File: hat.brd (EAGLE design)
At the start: 65 x 56.5 mm, 44 parts, among them U1 ADS1115IDGST, U2 ADXL345, U3 MCP2515-I/SO, U4 MCP2551, X1 16Mhz

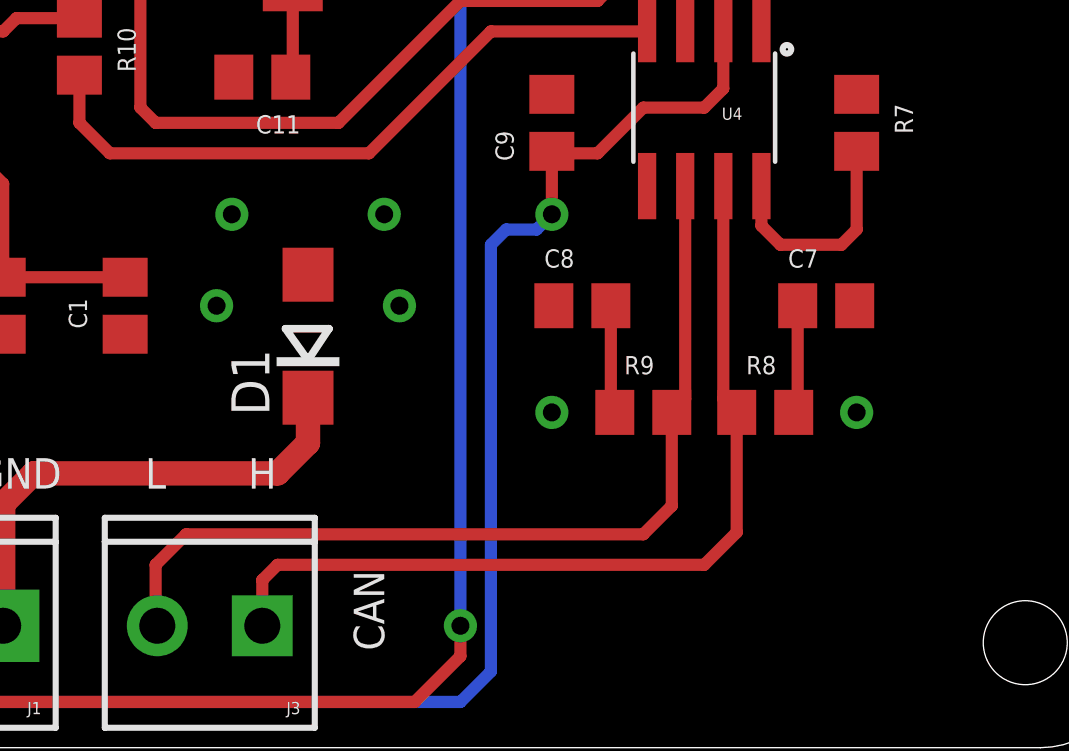
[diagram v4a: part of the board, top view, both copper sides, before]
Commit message: Tweaked spacing for two resistors
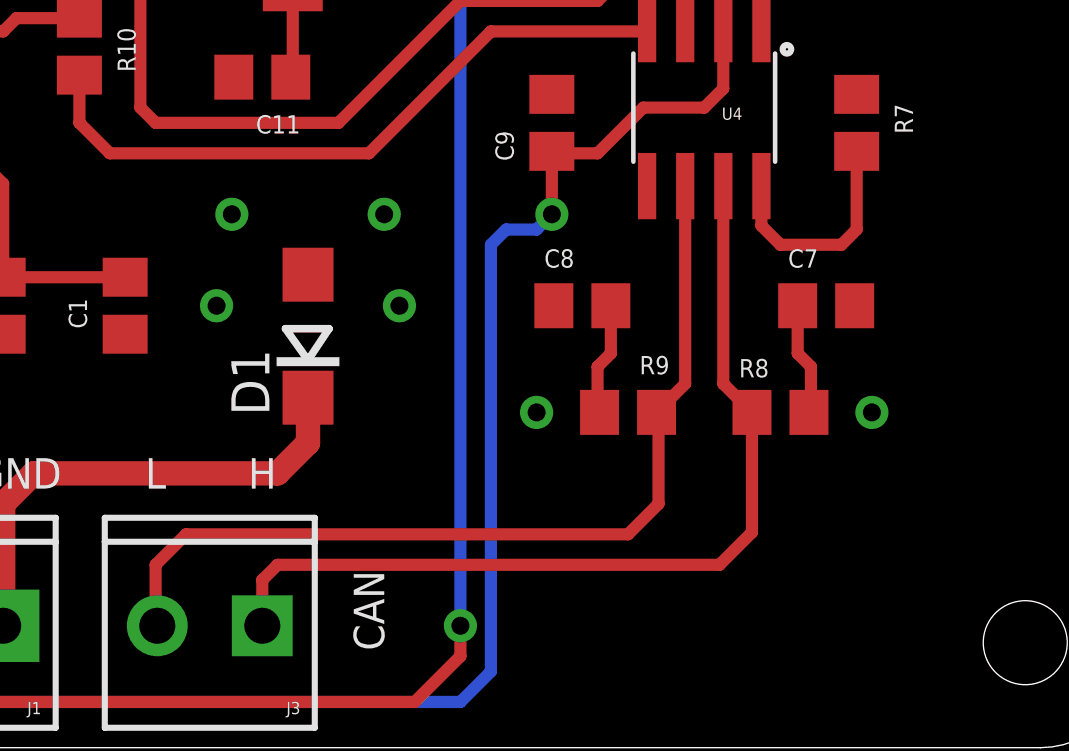
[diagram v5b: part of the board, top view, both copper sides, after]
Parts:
- moved R8 0.51 mm to (53.3, 11.2)
- moved R9 0.51 mm to (48.3, 11.2)
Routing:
- net CANH: track 29.7 -> 30.4 mm
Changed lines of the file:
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@@
 </element>
 <element name="R7" library="aceat64-passives" package="R0805" value="4k7" x="55.88" y="20.828" rot="R270"/>
-<element name="R8" library="aceat64-passives" package="R0805" value="100" x="52.832" y="11.176" smashed="yes" rot="R180">
-<attribute name="NAME" x="52.197" y="12.446" size="0.6096" layer="25"/>
-<attribute name="VALUE" x="52.197" y="9.906" size="0.6096" layer="27" align="top-left"/>
-</element>
-<element name="R9" library="aceat64-passives" package="R0805" value="100" x="48.768" y="11.176"/>
+<element name="R8" library="aceat64-passives" package="R0805" value="100" x="53.34" y="11.176" smashed="yes" rot="R180">
+<attribute name="NAME" x="52.959" y="12.954" size="0.6096" layer="25" rot="R180"/>
+<attribute name="VALUE" x="52.705" y="9.906" size="0.6096" layer="27" align="top-left"/>
+</element>
+<element name="R9" library="aceat64-passives" package="R0805" value="100" x="48.26" y="11.176" smashed="yes">
+<attribute name="NAME" x="48.641" y="12.446" size="0.6096" layer="25"/>
+<attribute name="VALUE" x="47.625" y="9.906" size="0.6096" layer="27" align="top-left"/>
+</element>
 <element name="FRAME2" library="SparkFun-Aesthetics" package="DUMMY" value="FRAME-LETTERNO_PACKAGE" x="0.508" y="0.508">
 <attribute name="DESIGNER" value="Nobody" x="0.508" y="0.508" size="1.778" layer="27" display="off"/>
@@
 <wire x1="8.636" y1="38.1" x2="8.636" y2="39.624" width="0.254" layer="1"/>
 <via x="6.096" y="16.764" extent="1-16" drill="0.6" shape="square"/>
-<via x="45.72" y="11.176" extent="1-16" drill="0.6" shape="square"/>
-<via x="55.88" y="11.176" extent="1-16" drill="0.6" shape="square"/>
+<via x="45.212" y="11.176" extent="1-16" drill="0.6" shape="square"/>
+<via x="56.388" y="11.176" extent="1-16" drill="0.6" shape="square"/>
 <via x="40.64" y="14.732" extent="1-16" drill="0.6" shape="square"/>
 <via x="51.308" y="40.64" extent="1-16" drill="0.6" shape="square"/>
@@
 <wire x1="36.068" y1="4.064" x2="36.068" y2="5.588" width="0.4064" layer="1"/>
 <wire x1="36.068" y1="5.588" x2="36.576" y2="6.096" width="0.4064" layer="1"/>
-<wire x1="36.576" y1="6.096" x2="50.8" y2="6.096" width="0.4064" layer="1"/>
-<wire x1="50.8" y1="6.096" x2="51.882" y2="7.178" width="0.4064" layer="1"/>
-<wire x1="51.882" y1="7.178" x2="51.882" y2="11.176" width="0.4064" layer="1"/>
-<wire x1="51.882" y1="11.176" x2="51.435" y2="11.623" width="0.4064" layer="1"/>
-<wire x1="51.435" y1="11.623" x2="51.435" y2="18.7198" width="0.4064" layer="1"/>
+<wire x1="36.576" y1="6.096" x2="51.308" y2="6.096" width="0.4064" layer="1"/>
+<wire x1="51.308" y1="6.096" x2="52.39" y2="7.178" width="0.4064" layer="1"/>
+<wire x1="52.39" y1="7.178" x2="52.39" y2="11.176" width="0.4064" layer="1"/>
+<wire x1="52.39" y1="11.176" x2="51.435" y2="12.131" width="0.4064" layer="1"/>
+<wire x1="51.435" y1="12.131" x2="51.435" y2="18.7198" width="0.4064" layer="1"/>
 </signal>
 <signal name="CANL">
@@
 <contactref element="R9" pad="2"/>
 <contactref element="J3" pad="2"/>
-<wire x1="48.768" y1="7.112" x2="33.528" y2="7.112" width="0.4064" layer="1"/>
 <wire x1="33.528" y1="7.112" x2="32.512" y2="6.096" width="0.4064" layer="1"/>
 <wire x1="32.512" y1="6.096" x2="32.512" y2="4.12" width="0.4064" layer="1"/>
 <wire x1="32.512" y1="4.12" x2="32.568" y2="4.064" width="0.4064" layer="1"/>
-<wire x1="48.768" y1="7.112" x2="49.718" y2="8.062" width="0.4064" layer="1"/>
-<wire x1="49.718" y1="8.062" x2="49.718" y2="11.176" width="0.4064" layer="1"/>
-<wire x1="49.718" y1="11.176" x2="50.165" y2="11.623" width="0.4064" layer="1"/>
-<wire x1="50.165" y1="11.623" x2="50.165" y2="18.7198" width="0.4064" layer="1"/>
+<wire x1="33.528" y1="7.112" x2="48.26" y2="7.112" width="0.4064" layer="1"/>
+<wire x1="48.26" y1="7.112" x2="49.276" y2="8.128" width="0.4064" layer="1"/>
+<wire x1="49.276" y1="8.128" x2="49.276" y2="11.11" width="0.4064" layer="1"/>
+<wire x1="49.276" y1="11.11" x2="49.21" y2="11.176" width="0.4064" layer="1"/>
+<wire x1="49.21" y1="11.176" x2="50.165" y2="12.131" width="0.4064" layer="1"/>
+<wire x1="50.165" y1="12.131" x2="50.165" y2="18.7198" width="0.4064" layer="1"/>
 </signal>
 <signal name="5V">
@@
 <signal name="N$6">
 <contactref element="R8" pad="1"/>
-<wire x1="53.782" y1="11.176" x2="53.914" y2="11.358" width="0.4064" layer="1"/>
+<wire x1="54.29" y1="11.176" x2="53.914" y2="11.358" width="0.4064" layer="1"/>
 <contactref element="C7" pad="1"/>
-<wire x1="53.782" y1="11.176" x2="53.914" y2="11.308" width="0.4064" layer="1"/>
-<wire x1="53.914" y1="11.308" x2="53.914" y2="14.732" width="0.4064" layer="1"/>
+<wire x1="53.914" y1="11.358" x2="54.356" y2="11.8" width="0.4064" layer="1"/>
+<wire x1="54.356" y1="11.8" x2="54.356" y2="12.7" width="0.4064" layer="1"/>
+<wire x1="54.356" y1="12.7" x2="53.914" y2="13.142" width="0.4064" layer="1"/>
+<wire x1="53.914" y1="13.142" x2="53.914" y2="14.732" width="0.4064" layer="1"/>
 </signal>
 <signal name="N$8">
 <contactref element="R9" pad="1"/>
-<wire x1="47.818" y1="11.176" x2="47.686" y2="11.358" width="0.4064" layer="1"/>
 <contactref element="C8" pad="1"/>
-<wire x1="47.686" y1="11.358" x2="47.686" y2="14.732" width="0.4064" layer="1"/>
+<wire x1="47.31" y1="11.176" x2="47.244" y2="11.242" width="0.4064" layer="1"/>
+<wire x1="47.244" y1="11.242" x2="47.244" y2="12.7" width="0.4064" layer="1"/>
+<wire x1="47.244" y1="12.7" x2="47.686" y2="13.142" width="0.4064" layer="1"/>
+<wire x1="47.686" y1="13.142" x2="47.686" y2="14.732" width="0.4064" layer="1"/>
 </signal>
 <signal name="N$4">

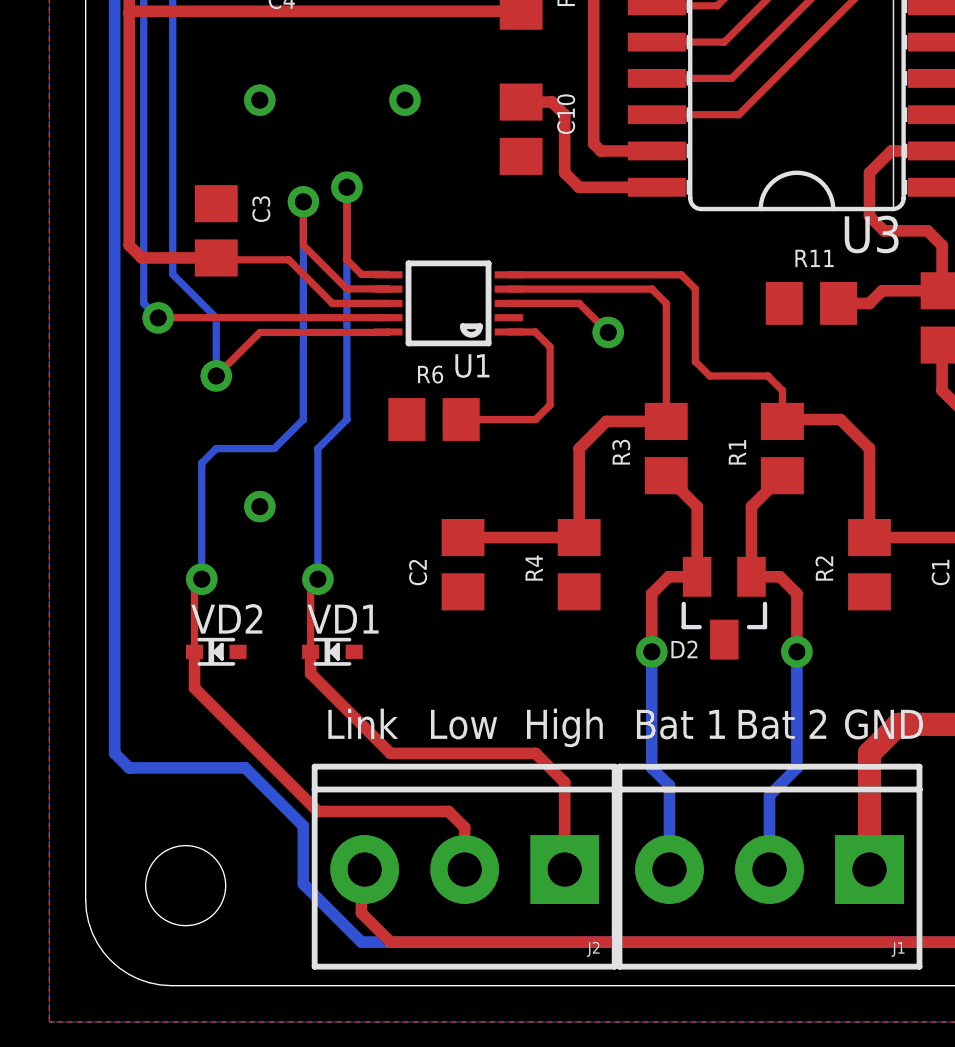
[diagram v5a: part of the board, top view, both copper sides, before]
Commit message: Replaced TVS diodes VD1/VD2 with single TVS diode D3
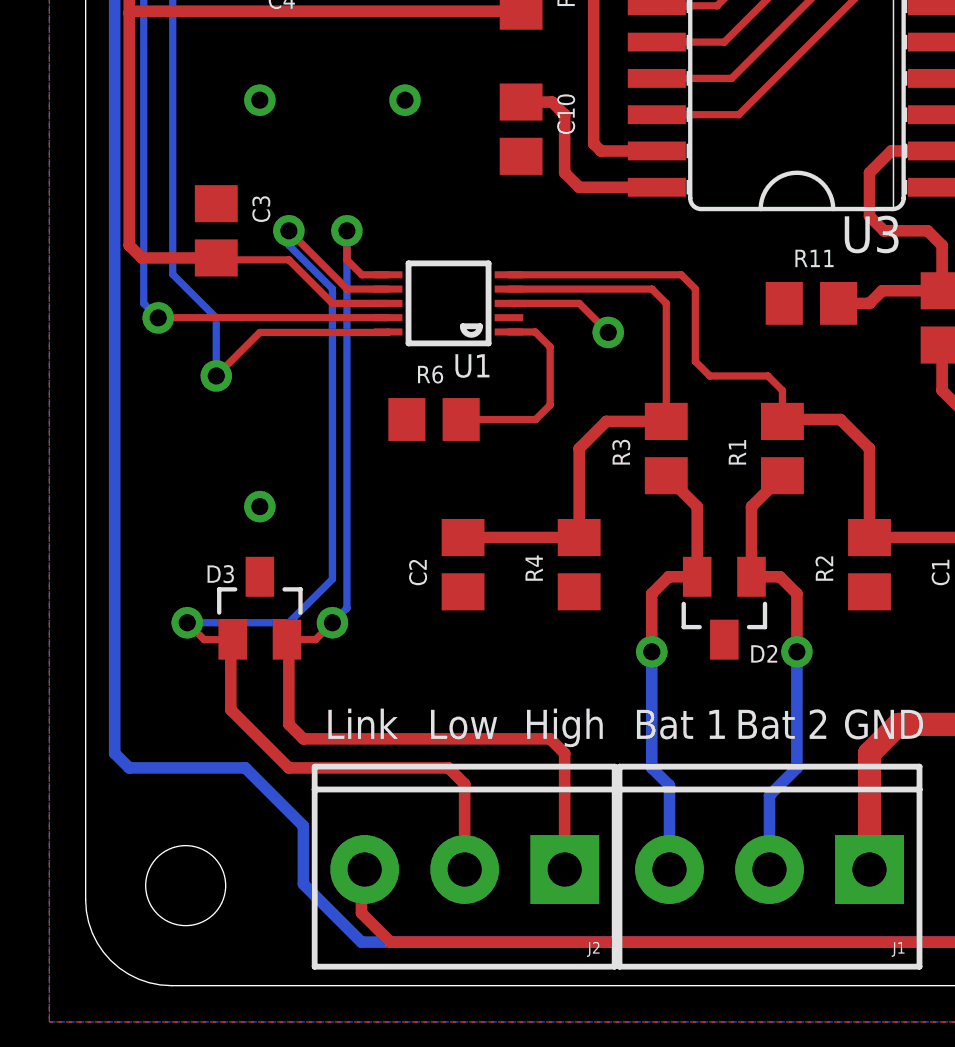
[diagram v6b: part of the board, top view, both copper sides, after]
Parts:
- removed VD1, VD2: (no value), diode:SOD523
- added D3: (no value), diode:SOT23
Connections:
- net GND: now also D3.3; no longer VD1.A, VD2.A
- net SHUNT-HIGH-INPUT: now also D3.2; no longer VD1.C
- net SHUNT-LOW-INPUT: now also D3.1; no longer VD2.C
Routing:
- net SHUNT-LOW-INPUT: track 37.9 -> 39.4 mm
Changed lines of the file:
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@@
 <element name="GPS" library="SparkFun-Connectors" package="1X05" value="" x="61.468" y="46.482" rot="R270"/>
 <element name="U2" library="SparkFun-Sensors" package="LGA14" value="ADXL345" x="11.684" y="40.64" rot="R90"/>
-<element name="U1" library="microbuilder" package="MSOP10" value="ADS1115IDGST" x="12.7" y="23.876" rot="R90"/>
+<element name="U1" library="microbuilder" package="MSOP10" value="ADS1115IDGST" x="12.7" y="23.876" smashed="yes" rot="R90">
+<attribute name="NAME" x="14.224" y="22.098" size="0.8128" layer="25" ratio="10" rot="R180"/>
+<attribute name="VALUE" x="10.16" y="25.908" size="0.8128" layer="27" ratio="10"/>
+</element>
 <element name="R5" library="aceat64-passives" package="R0805" value="4k7" x="42.672" y="33.02" rot="R90"/>
 <element name="R1" library="aceat64-resistor" package="R0805" value="4k7" x="24.384" y="18.796" rot="R90"/>
@@
 <element name="U3" library="mcp2515" package="SO18L" value="MCP2515-I/SO" x="24.892" y="33.02" rot="R90"/>
 <element name="D2" library="diode" package="SOT23" value="" x="22.352" y="13.208" smashed="yes" rot="R180">
-<attribute name="NAME" x="20.955" y="12.065" size="0.6096" layer="25" align="top-center"/>
+<attribute name="NAME" x="23.749" y="11.303" size="0.6096" layer="25" rot="R180" align="top-center"/>
 <attribute name="VALUE" x="24.257" y="16.383" size="1.27" layer="27" rot="R180"/>
 </element>
-<element name="VD1" library="diode" package="SOD523" value="" x="8.636" y="11.684"/>
-<element name="VD2" library="diode" package="SOD523" value="" x="4.572" y="11.684"/>
 <element name="J1" library="SparkFun-Connectors" package="SCREWTERMINAL-3.5MM-3" value="" x="27.432" y="4.064" rot="R180">
 <attribute name="PROD_ID" value="CONN-08288" x="27.432" y="4.064" size="1.778" layer="27" rot="R180" display="off"/>
@@
 <element name="C11" library="aceat64-passives" package="C0805" value="22pF" x="36.068" y="22.352" rot="R180"/>
 <element name="C12" library="aceat64-passives" package="C0805" value="22pF" x="36.068" y="40.64" rot="R180"/>
+<element name="D3" library="diode" package="SOT23" value="" x="6.096" y="13.208" smashed="yes">
+<attribute name="NAME" x="4.191" y="14.097" size="0.6096" layer="25"/>
+<attribute name="VALUE" x="4.191" y="10.033" size="1.27" layer="27"/>
+</element>
 </elements>
 <signals>
@@
 <via x="34.544" y="14.732" extent="1-16" drill="0.6" shape="square"/>
 <contactref element="D2" pad="3"/>
-<contactref element="VD2" pad="A"/>
-<contactref element="VD1" pad="A"/>
 <via x="8.636" y="38.1" extent="1-16" drill="0.6" shape="square"/>
 <via x="4.572" y="43.18" extent="1-16" drill="0.6" shape="square"/>
@@
 <contactref element="C11" pad="2"/>
 <contactref element="C12" pad="2"/>
+<contactref element="D3" pad="3"/>
 </signal>
 <signal name="TXD">
@@
 <signal name="SHUNT-HIGH-INPUT">
 <contactref element="U1" pad="6"/>
-<contactref element="VD1" pad="C"/>
-<wire x1="10.5869" y1="24.876" x2="10.5709" y2="24.892" width="0.254" layer="1"/>
-<wire x1="10.5709" y1="24.892" x2="9.652" y2="24.892" width="0.254" layer="1"/>
-<wire x1="9.652" y1="24.892" x2="9.144" y2="25.4" width="0.254" layer="1"/>
-<wire x1="9.144" y1="25.4" x2="9.144" y2="27.94" width="0.254" layer="1"/>
-<via x="9.144" y="27.94" extent="1-16" drill="0.6"/>
-<wire x1="9.144" y1="27.94" x2="9.144" y2="19.812" width="0.254" layer="16"/>
-<wire x1="9.144" y1="19.812" x2="8.128" y2="18.796" width="0.254" layer="16"/>
-<wire x1="8.128" y1="18.796" x2="8.128" y2="14.224" width="0.254" layer="16"/>
-<via x="8.128" y="14.224" extent="1-16" drill="0.6"/>
-<wire x1="8.128" y1="14.224" x2="7.874" y2="13.97" width="0.254" layer="1"/>
-<wire x1="7.874" y1="13.97" x2="7.874" y2="11.684" width="0.254" layer="1"/>
 <contactref element="J2" pad="1"/>
-<wire x1="7.874" y1="11.684" x2="7.874" y2="10.922" width="0.4064" layer="1"/>
-<wire x1="7.874" y1="10.922" x2="10.668" y2="8.128" width="0.4064" layer="1"/>
-<wire x1="10.668" y1="8.128" x2="15.748" y2="8.128" width="0.4064" layer="1"/>
-<wire x1="15.748" y1="8.128" x2="16.764" y2="7.112" width="0.4064" layer="1"/>
-<wire x1="16.764" y1="7.112" x2="16.764" y2="4.064" width="0.4064" layer="1"/>
+<contactref element="D3" pad="2"/>
+<wire x1="16.764" y1="4.064" x2="16.764" y2="8.128" width="0.4064" layer="1"/>
+<wire x1="16.764" y1="8.128" x2="16.256" y2="8.636" width="0.4064" layer="1"/>
+<wire x1="16.256" y1="8.636" x2="7.62" y2="8.636" width="0.4064" layer="1"/>
+<wire x1="7.62" y1="8.636" x2="7.112" y2="9.144" width="0.4064" layer="1"/>
+<wire x1="7.112" y1="9.144" x2="7.112" y2="12.042" width="0.4064" layer="1"/>
+<wire x1="7.112" y1="12.042" x2="7.046" y2="12.108" width="0.4064" layer="1"/>
+<wire x1="10.5869" y1="24.876" x2="9.668" y2="24.876" width="0.254" layer="1"/>
+<wire x1="9.668" y1="24.876" x2="9.144" y2="25.4" width="0.254" layer="1"/>
+<wire x1="9.144" y1="25.4" x2="9.144" y2="26.416" width="0.254" layer="1"/>
+<via x="9.144" y="26.416" extent="1-16" drill="0.6"/>
+<wire x1="9.144" y1="26.416" x2="9.144" y2="13.208" width="0.254" layer="16"/>
+<wire x1="9.144" y1="13.208" x2="8.636" y2="12.7" width="0.254" layer="16"/>
+<via x="8.636" y="12.7" extent="1-16" drill="0.6"/>
+<wire x1="8.636" y1="12.7" x2="8.044" y2="12.108" width="0.254" layer="1"/>
+<wire x1="8.044" y1="12.108" x2="7.046" y2="12.108" width="0.254" layer="1"/>
 </signal>
 <signal name="SHUNT-LOW-INPUT">
 <contactref element="U1" pad="7"/>
-<contactref element="VD2" pad="C"/>
-<wire x1="10.5869" y1="24.376" x2="10.5789" y2="24.384" width="0.254" layer="1"/>
-<wire x1="10.5789" y1="24.384" x2="9.144" y2="24.384" width="0.254" layer="1"/>
-<wire x1="9.144" y1="24.384" x2="7.62" y2="25.908" width="0.254" layer="1"/>
-<wire x1="7.62" y1="25.908" x2="7.62" y2="27.432" width="0.254" layer="1"/>
-<via x="7.62" y="27.432" extent="1-16" drill="0.6"/>
-<wire x1="7.62" y1="27.432" x2="7.62" y2="19.812" width="0.254" layer="16"/>
-<wire x1="7.62" y1="19.812" x2="6.604" y2="18.796" width="0.254" layer="16"/>
-<wire x1="6.604" y1="18.796" x2="4.572" y2="18.796" width="0.254" layer="16"/>
-<wire x1="4.572" y1="18.796" x2="4.064" y2="18.288" width="0.254" layer="16"/>
-<wire x1="4.064" y1="18.288" x2="4.064" y2="14.224" width="0.254" layer="16"/>
-<via x="4.064" y="14.224" extent="1-16" drill="0.6"/>
-<wire x1="4.064" y1="14.224" x2="3.81" y2="13.97" width="0.254" layer="1"/>
-<wire x1="3.81" y1="13.97" x2="3.81" y2="11.684" width="0.254" layer="1"/>
 <contactref element="J2" pad="2"/>
-<wire x1="13.264" y1="4.064" x2="13.264" y2="5.532" width="0.4064" layer="1"/>
-<wire x1="13.264" y1="5.532" x2="12.7" y2="6.096" width="0.4064" layer="1"/>
-<wire x1="12.7" y1="6.096" x2="8.128" y2="6.096" width="0.4064" layer="1"/>
-<wire x1="8.128" y1="6.096" x2="3.81" y2="10.414" width="0.4064" layer="1"/>
-<wire x1="3.81" y1="10.414" x2="3.81" y2="11.684" width="0.4064" layer="1"/>
+<contactref element="D3" pad="1"/>
+<wire x1="13.264" y1="4.064" x2="13.264" y2="7.056" width="0.4064" layer="1"/>
+<wire x1="13.264" y1="7.056" x2="12.7" y2="7.62" width="0.4064" layer="1"/>
+<wire x1="12.7" y1="7.62" x2="7.112" y2="7.62" width="0.4064" layer="1"/>
+<wire x1="7.112" y1="7.62" x2="5.08" y2="9.652" width="0.4064" layer="1"/>
+<wire x1="5.08" y1="9.652" x2="5.08" y2="12.042" width="0.4064" layer="1"/>
+<wire x1="5.08" y1="12.042" x2="5.146" y2="12.108" width="0.4064" layer="1"/>
+<wire x1="10.5869" y1="24.376" x2="9.152" y2="24.376" width="0.254" layer="1"/>
+<wire x1="9.152" y1="24.376" x2="7.112" y2="26.416" width="0.254" layer="1"/>
+<via x="7.112" y="26.416" extent="1-16" drill="0.6"/>
+<wire x1="7.112" y1="26.416" x2="7.112" y2="25.908" width="0.254" layer="16"/>
+<wire x1="7.112" y1="25.908" x2="8.636" y2="24.384" width="0.254" layer="16"/>
+<wire x1="5.146" y1="12.108" x2="4.148" y2="12.108" width="0.254" layer="1"/>
+<wire x1="4.148" y1="12.108" x2="3.556" y2="12.7" width="0.254" layer="1"/>
+<via x="3.556" y="12.7" extent="1-16" drill="0.6"/>
+<wire x1="3.556" y1="12.7" x2="7.112" y2="12.7" width="0.254" layer="16"/>
+<wire x1="7.112" y1="12.7" x2="8.636" y2="14.224" width="0.254" layer="16"/>
+<wire x1="8.636" y1="14.224" x2="8.636" y2="24.384" width="0.254" layer="16"/>
 </signal>
 <signal name="LINKED-INPUT">
